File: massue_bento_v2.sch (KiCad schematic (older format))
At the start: 20 parts

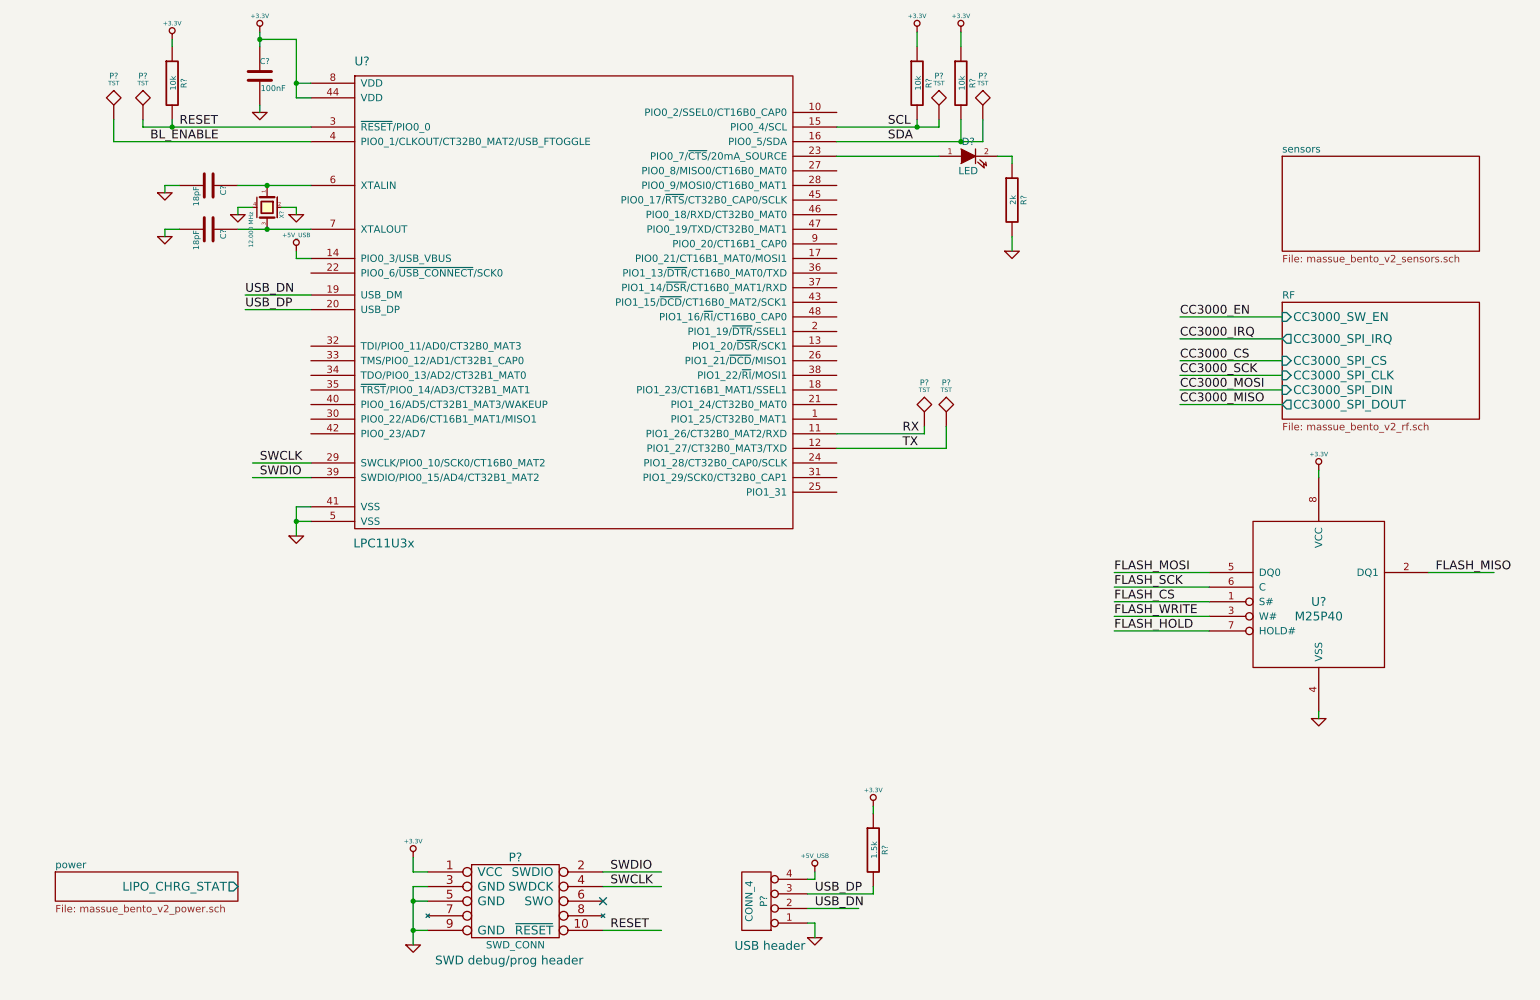
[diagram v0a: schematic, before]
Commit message: New: end of the MCU connections, SPI ports connections, battery monitor circuit and LED headers
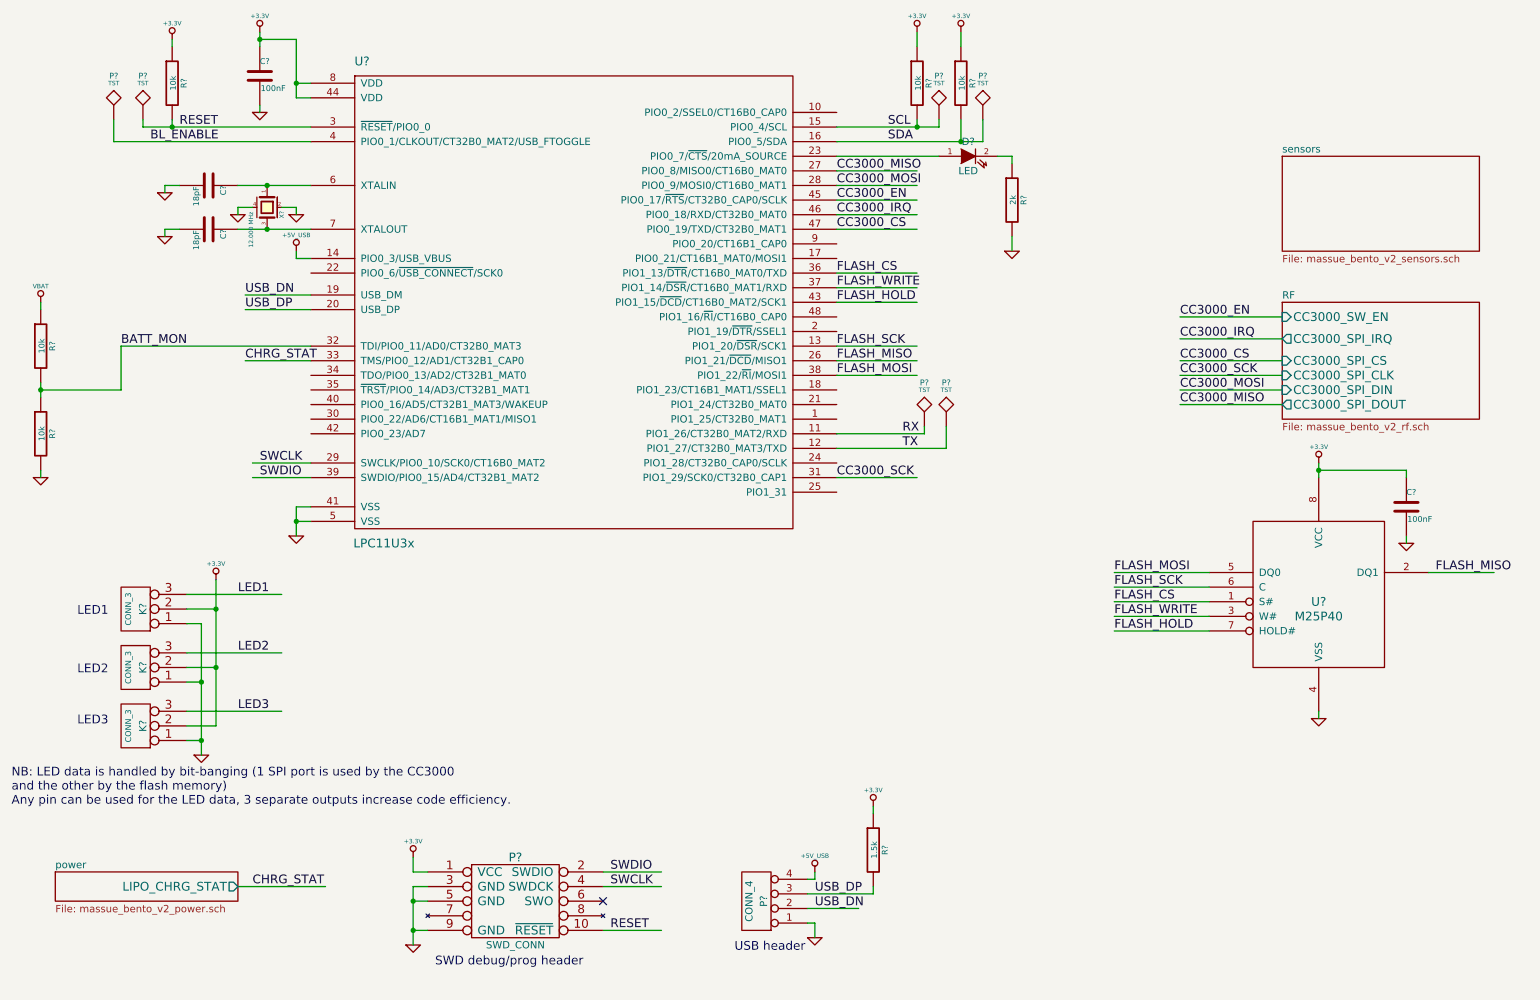
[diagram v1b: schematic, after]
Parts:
- added C?: 100nF, symbol C
- added K? (x3): CONN_3, symbol CONN_3
- added R? (x2): 10k, symbol R
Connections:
- net labels added: BATT_MON, CHRG_STAT, LED1, LED2, LED3, VBAT
- wire segments 78 -> 112
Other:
- note added: "LED1"
- note added: "LED2"
- note added: "LED3"
- note added: "NB: LED data is handled by bit-banging (1 SPI port is used by the CC3000\nand the other by the flash memory)\nAny pin can be used for the LED data, 3 separate outputs increase code efficiency."

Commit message: Fix: global annotation, fixed bugs to satisfy ERC
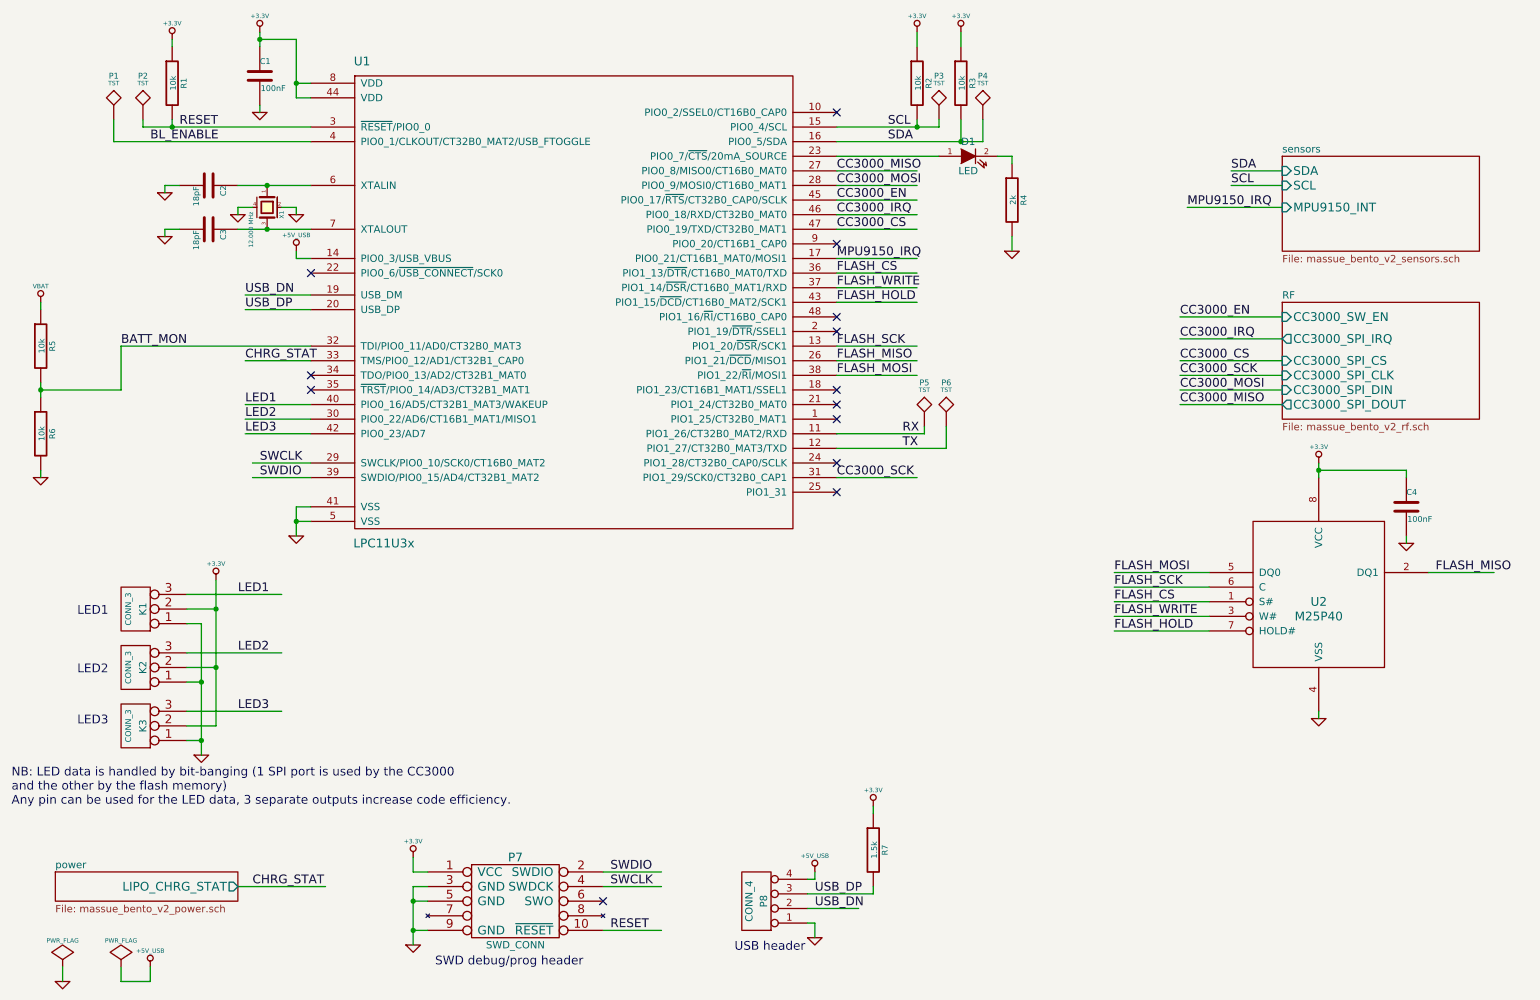
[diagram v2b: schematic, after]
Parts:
- gave numbers to parts that had none: 26
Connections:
- net labels added: MPU9150_IRQ
- wire segments 112 -> 123
- no-connect marks 1 -> 13

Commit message: New : AT42 sensor
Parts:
- added R19, R20: 10k, symbol R
- renumbered C2 to C1, C3 to C2, C1 to C3, P7 to P3, P8 to P4, P3 to P6, P6 to P7, P4 to P8, R5 to R1, R6 to R2, R1 to R3, R7 to R4, R2 to R5, R3 to R6, R4 to R7
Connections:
- wire segments 123 -> 128
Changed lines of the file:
@@
 EESchema Schematic File Version 2
 LIBS:power
+LIBS:tom_kicad
 LIBS:device
-LIBS:transistors
 LIBS:conn
-LIBS:linear
-LIBS:regul
-LIBS:74xx
-LIBS:cmos4000
-LIBS:adc-dac
-LIBS:memory
-LIBS:xilinx
-LIBS:special
-LIBS:microcontrollers
-LIBS:dsp
-LIBS:microchip
-LIBS:analog_switches
-LIBS:motorola
-LIBS:texas
-LIBS:intel
-LIBS:audio
-LIBS:interface
-LIBS:digital-audio
-LIBS:philips
-LIBS:display
-LIBS:cypress
-LIBS:siliconi
-LIBS:opto
-LIBS:atmel
-LIBS:contrib
-LIBS:valves
-LIBS:tom_kicad
 LIBS:massue_bento_v2-cache
 EELAYER 24 0
@@
 F3 "SCL" I L 9300 2150 60
 F4 "MPU9150_INT" I L 9300 2300 60
+F5 "AT42_INT" I L 9300 2450 60
 $EndSheet
 $Comp
@@
 $EndComp
 $Comp
-L CONN_4 P8
+L CONN_4 P4
 U 1 1 53A5B8F1
 P 5700 7050
-F 0 "P8" V 5650 7050 50  0000 C CNN
+F 0 "P4" V 5650 7050 50  0000 C CNN
 F 1 "CONN_4" V 5750 7050 50  0000 C CNN
 F 2 "" H 5700 7050 60  0000 C CNN
@@
 	2550 1550 2650 1550
 $Comp
-L R R1
+L R R3
 U 1 1 53A5BF5B
 P 1700 1450
-F 0 "R1" V 1780 1450 40  0000 C CNN
+F 0 "R3" V 1780 1450 40  0000 C CNN
 F 1 "10k" V 1707 1451 40  0000 C CNN
 F 2 "" V 1630 1450 30  0000 C CNN
@@
 	1700 1150 1700 1200
 $Comp
-L C C1
+L C C3
 U 1 1 53A5CC0B
 P 2300 1400
-F 0 "C1" H 2300 1500 40  0000 L CNN
+F 0 "C3" H 2300 1500 40  0000 L CNN
 F 1 "100nF" H 2306 1315 40  0000 L CNN
 F 2 "" H 2338 1250 30  0000 C CNN
@@
 	2150 2300 2250 2300
 $Comp
-L C C2
+L C C1
 U 1 1 53A5D2B5
 P 1950 2150
-F 0 "C2" H 1950 2250 40  0000 L CNN
+F 0 "C1" H 1950 2250 40  0000 L CNN
 F 1 "18pF" H 1956 2065 40  0000 L CNN
 F 2 "" H 1988 2000 30  0000 C CNN
@@
 $EndComp
 $Comp
-L C C3
+L C C2
 U 1 1 53A5D362
 P 1950 2450
-F 0 "C3" H 1950 2550 40  0000 L CNN
+F 0 "C2" H 1950 2550 40  0000 L CNN
 F 1 "18pF" H 1956 2365 40  0000 L CNN
 F 2 "" H 1988 2300 30  0000 C CNN
@@
 	2550 2650 2650 2650
 $Comp
-L R R7
+L R R4
 U 1 1 53A5DF87
 P 6500 6700
-F 0 "R7" V 6580 6700 40  0000 C CNN
+F 0 "R4" V 6580 6700 40  0000 C CNN
 F 1 "1.5k" V 6507 6701 40  0000 C CNN
 F 2 "" V 6430 6700 30  0000 C CNN
@@
 Connection ~ 2550 4450
 $Comp
-L SWD_CONN P7
+L SWD_CONN P3
 U 1 1 53A60624
 P 4050 7050
-F 0 "P7" H 4050 7350 60  0000 C CNN
+F 0 "P3" H 4050 7350 60  0000 C CNN
 F 1 "SWD_CONN" H 4050 6750 50  0000 C CNN
 F 2 "" H 4050 7050 60  0000 C CNN
@@
 NoConn ~ 4650 7050
 $Comp
-L R R2
+L R R5
 U 1 1 53A61B1D
 P 6800 1450
-F 0 "R2" V 6880 1450 40  0000 C CNN
+F 0 "R5" V 6880 1450 40  0000 C CNN
 F 1 "10k" V 6807 1451 40  0000 C CNN
 F 2 "" V 6730 1450 30  0000 C CNN
@@
 $EndComp
 $Comp
-L R R3
+L R R6
 U 1 1 53A61B66
 P 7100 1450
-F 0 "R3" V 7180 1450 40  0000 C CNN
+F 0 "R6" V 7180 1450 40  0000 C CNN
 F 1 "10k" V 7107 1451 40  0000 C CNN
 F 2 "" V 7030 1450 30  0000 C CNN
@@
 $EndComp
 $Comp
-L R R4
+L R R7
 U 1 1 53A62059
 P 7450 2250
-F 0 "R4" V 7530 2250 40  0000 C CNN
+F 0 "R7" V 7530 2250 40  0000 C CNN
 F 1 "2k" V 7457 2251 40  0000 C CNN
 F 2 "" V 7380 2250 30  0000 C CNN
@@
 $EndComp
 $Comp
-L TST P6
+L TST P7
 U 1 1 53A6533B
 P 7000 3800
-F 0 "P6" H 7000 4100 40  0000 C CNN
+F 0 "P7" H 7000 4100 40  0000 C CNN
 F 1 "TST" H 7000 4050 30  0000 C CNN
 F 2 "" H 7000 3800 60  0000 C CNN
@@
 $EndComp
 $Comp
-L TST P3
+L TST P6
 U 1 1 53A66F4E
 P 6950 1700
-F 0 "P3" H 6950 2000 40  0000 C CNN
+F 0 "P6" H 6950 2000 40  0000 C CNN
 F 1 "TST" H 6950 1950 30  0000 C CNN
 F 2 "" H 6950 1700 60  0000 C CNN
@@
 $EndComp
 $Comp
-L TST P4
+L TST P8
 U 1 1 53A673E3
 P 7250 1700
-F 0 "P4" H 7250 2000 40  0000 C CNN
+F 0 "P8" H 7250 2000 40  0000 C CNN
 F 1 "TST" H 7250 1950 30  0000 C CNN
 F 2 "" H 7250 1700 60  0000 C CNN
@@
 $EndComp
 $Comp
-L R R5
+L R R1
 U 1 1 53A7508F
 P 800 3250
-F 0 "R5" V 880 3250 40  0000 C CNN
+F 0 "R1" V 880 3250 40  0000 C CNN
 F 1 "10k" V 807 3251 40  0000 C CNN
 F 2 "" V 730 3250 30  0000 C CNN
@@
 $EndComp
 $Comp
-L R R6
+L R R2
 U 1 1 53A751A1
 P 800 3850
-F 0 "R6" V 880 3850 40  0000 C CNN
+F 0 "R2" V 880 3850 40  0000 C CNN
 F 1 "10k" V 807 3851 40  0000 C CNN
 F 2 "" V 730 3850 30  0000 C CNN
@@
 NoConn ~ 6250 3150
 Wire Wire Line
-	8950 2050 9300 2050
-Wire Wire Line
-	8950 2150 9300 2150
+	8300 2050 9300 2050
+Wire Wire Line
+	8300 2150 9300 2150
 Text Label 8950 2050 0    60   ~ 0
 SDA
@@
 Text Label 6250 2650 0    60   ~ 0
 MPU9150_IRQ
+Wire Wire Line
+	9300 2450 8650 2450
+$Comp
+L +3.3V #PWR029
+U 1 1 53A74227
+P 8600 1400
+F 0 "#PWR029" H 8600 1360 30  0001 C CNN
+F 1 "+3.3V" H 8600 1510 30  0000 C CNN
+F 2 "" H 8600 1400 60  0000 C CNN
+F 3 "" H 8600 1400 60  0000 C CNN
+	1    8600 1400
+	1    0    0    -1
+$EndComp
+$Comp
+L R R20
+U 1 1 53A74253
+P 8750 1700
+F 0 "R20" V 8830 1700 40  0000 C CNN
+F 1 "10k" V 8757 1701 40  0000 C CNN
+F 2 "" V 8680 1700 30  0000 C CNN
+F 3 "" H 8750 1700 30  0000 C CNN
+	1    8750 1700
+	1    0    0    -1
+$EndComp
+$Comp
+L R R19
+U 1 1 53A742AA
+P 8600 1700
+F 0 "R19" V 8680 1700 40  0000 C CNN
+F 1 "10k" V 8607 1701 40  0000 C CNN
+F 2 "" V 8530 1700 30  0000 C CNN
+F 3 "" H 8600 1700 30  0000 C CNN
+	1    8600 1700
+	1    0    0    -1
+$EndComp
+Wire Wire Line
+	8600 1400 8600 1450
+Wire Wire Line
+	8600 1450 8750 1450
+Wire Wire Line
+	8750 1950 8750 2050
+Connection ~ 8750 2050
+Wire Wire Line
+	8600 1950 8600 2150
+Connection ~ 8600 2150
 $EndSCHEMATC

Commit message: Fix : pull up for I2C and AT42INT connection
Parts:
- removed R19, R20: 10k, symbol R
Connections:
- net labels added: AT42_INT
- wire segments 128 -> 125
- no-connect marks 13 -> 12
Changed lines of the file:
@@
 NoConn ~ 2650 3450
 NoConn ~ 2650 3550
-NoConn ~ 6250 4250
 NoConn ~ 6250 4050
 NoConn ~ 6250 3750
@@
 Wire Wire Line
 	9300 2450 8650 2450
-$Comp
-L +3.3V #PWR029
-U 1 1 53A74227
-P 8600 1400
-F 0 "#PWR029" H 8600 1360 30  0001 C CNN
-F 1 "+3.3V" H 8600 1510 30  0000 C CNN
-F 2 "" H 8600 1400 60  0000 C CNN
-F 3 "" H 8600 1400 60  0000 C CNN
-	1    8600 1400
-	1    0    0    -1
-$EndComp
-$Comp
-L R R20
-U 1 1 53A74253
-P 8750 1700
-F 0 "R20" V 8830 1700 40  0000 C CNN
-F 1 "10k" V 8757 1701 40  0000 C CNN
-F 2 "" V 8680 1700 30  0000 C CNN
-F 3 "" H 8750 1700 30  0000 C CNN
-	1    8750 1700
-	1    0    0    -1
-$EndComp
-$Comp
-L R R19
-U 1 1 53A742AA
-P 8600 1700
-F 0 "R19" V 8680 1700 40  0000 C CNN
-F 1 "10k" V 8607 1701 40  0000 C CNN
-F 2 "" V 8530 1700 30  0000 C CNN
-F 3 "" H 8600 1700 30  0000 C CNN
-	1    8600 1700
-	1    0    0    -1
-$EndComp
+Text Label 8650 2450 0    60   ~ 0
+AT42_INT
 Wire Wire Line
-	8600 1400 8600 1450
-Wire Wire Line
-	8600 1450 8750 1450
-Wire Wire Line
-	8750 1950 8750 2050
-Connection ~ 8750 2050
-Wire Wire Line
-	8600 1950 8600 2150
-Connection ~ 8600 2150
+	6250 4250 6800 4250
+Text Label 6500 4250 0    60   ~ 0
+AT42_INT
 $EndSCHEMATC

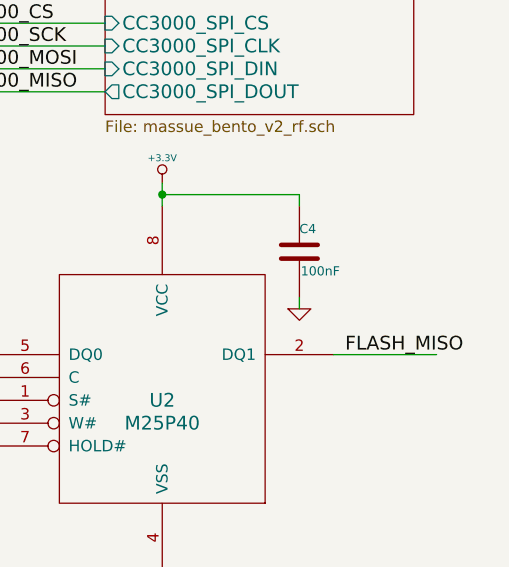
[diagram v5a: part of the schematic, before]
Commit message: Clean: remove unnecessary pull-up resistor (integrated in MCU)
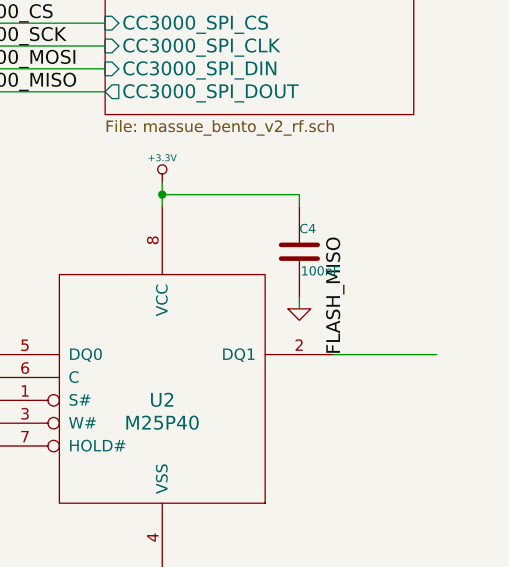
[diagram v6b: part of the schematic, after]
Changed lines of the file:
@@
 Wire Wire Line
 	10300 4800 10750 4800
-Text Label 10350 4800 0    60   ~ 0
+Text Label 10350 4800 1    60   ~ 0
 FLASH_MISO
 Wire Wire Line
